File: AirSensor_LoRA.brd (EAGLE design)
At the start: 37.8 x 29.7 mm, 6 parts, among them U2 RFM95W-915S2

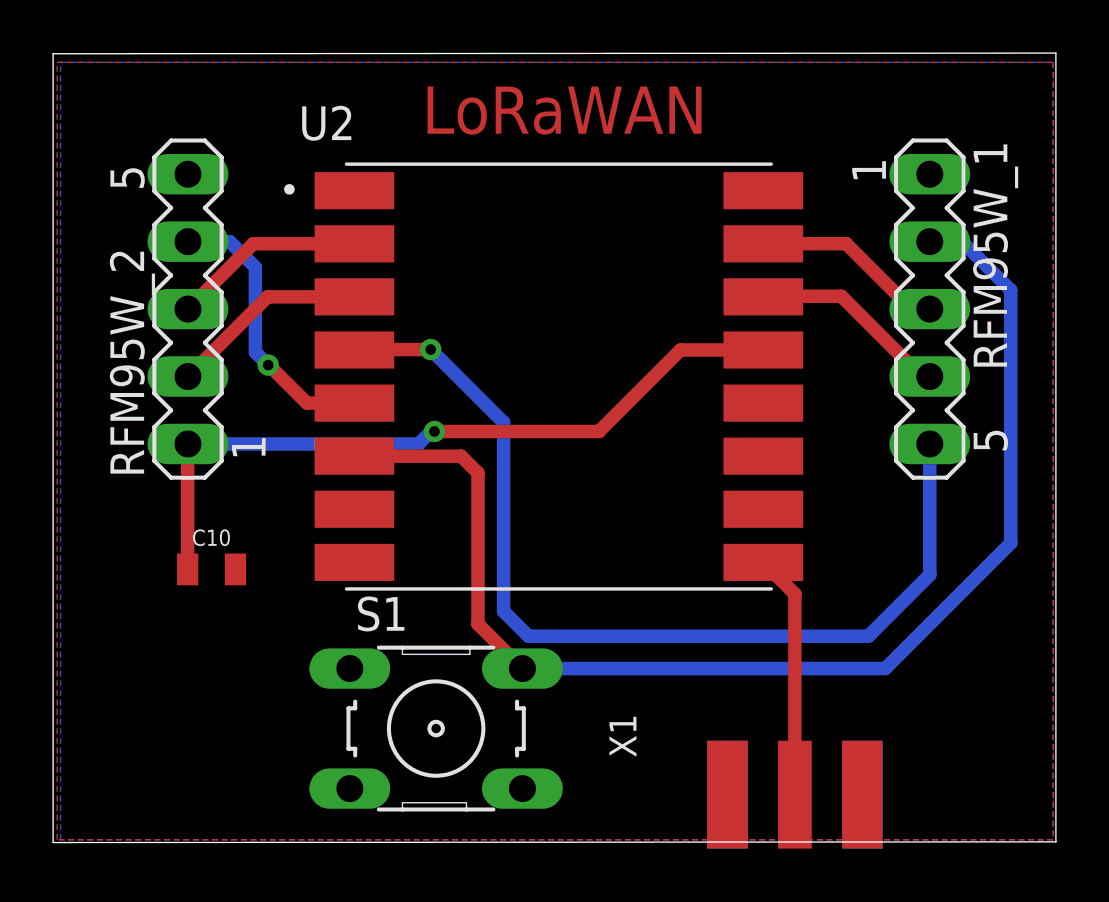
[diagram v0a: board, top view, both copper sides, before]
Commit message: added JTAG schematic and PCB  + all pictures
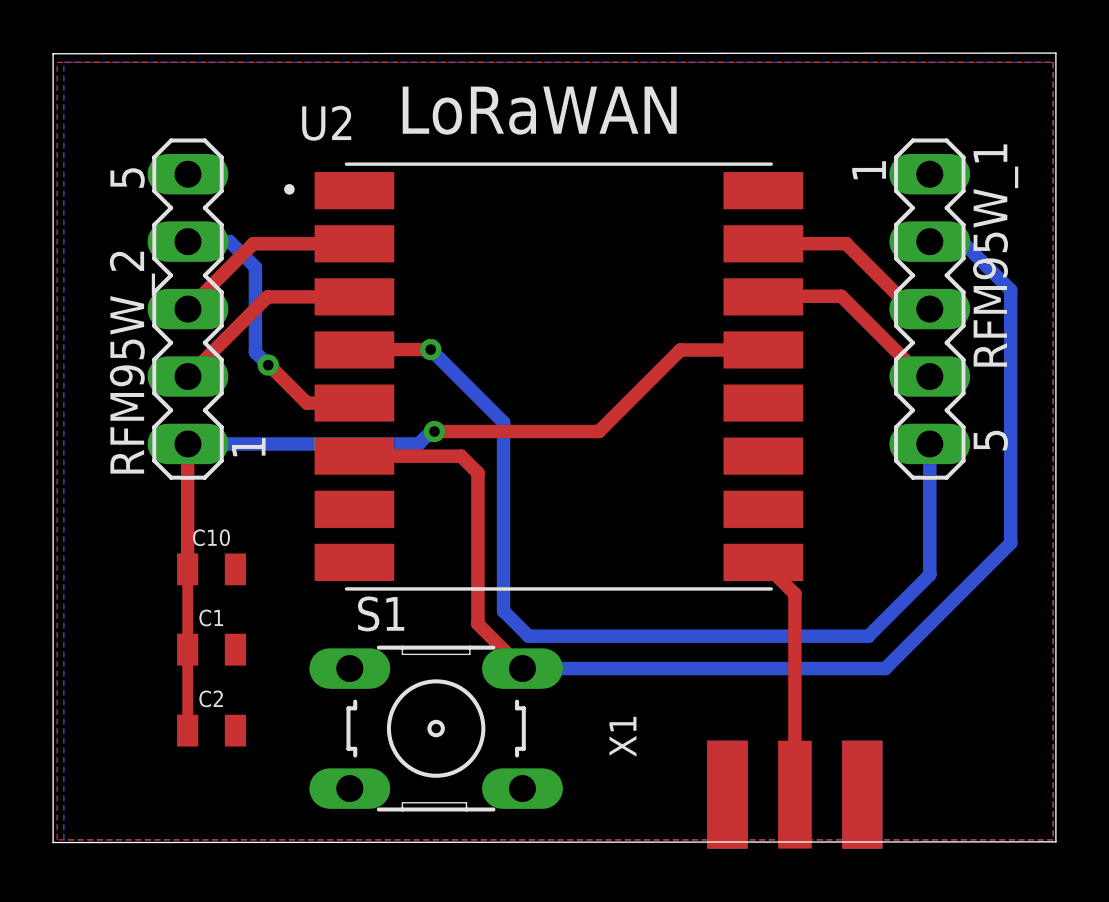
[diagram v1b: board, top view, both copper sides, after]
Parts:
- added C1: 1uF, SparkFun-Capacitors:0805
- added C2: 10uF, SparkFun-Capacitors:0805
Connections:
- net GND: now also C1.2, C2.2
- net N$17: now also C1.1, C2.1
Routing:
- net N$17: track 27.9 -> 34.0 mm
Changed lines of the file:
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@@
 <setting verticaltext="up"/>
 </settings>
-<grid distance="10" unitdist="mil" unit="mil" style="dots" multiple="1" display="yes" altdistance="5" altunitdist="mil" altunit="mm"/>
+<grid distance="5" unitdist="mil" unit="mil" style="dots" multiple="1" display="yes" altdistance="5" altunitdist="mil" altunit="mm"/>
 <layers>
 <layer number="1" name="Top" color="4" fill="1" visible="yes" active="yes"/>
@@
 <layer number="43" name="vRestrict" color="2" fill="10" visible="yes" active="yes"/>
 <layer number="44" name="Drills" color="7" fill="1" visible="no" active="yes"/>
-<layer number="45" name="Holes" color="7" fill="1" visible="no" active="yes"/>
+<layer number="45" name="Holes" color="7" fill="1" visible="yes" active="yes"/>
 <layer number="46" name="Milling" color="3" fill="1" visible="no" active="yes"/>
 <layer number="47" name="Measures" color="7" fill="1" visible="no" active="yes"/>
@@
 </layers>
 <board>
+<fusionsync huburn="a.YnVzaW5lc3M6c2t5bmV0MTMz" projecturn="a.YnVzaW5lc3M6c2t5bmV0MTMzI0QyMDE5MTAzMTIzMzQxNDY3Ng" f3durn="urn:adsk.wipprod:dm.lineage:gBG1N-XqQO-DzMLJpc-8hg" pcbguid="713ceda1-754c-4077-b978-a9e63d735a61" lastpulledtime="" lastsyncedchangeguid="" latestrevisionid="c9c4a9db-c59c-4e5b-af83-e9ca314a6cc9" lastsyncedrevisionid="c9c4a9db-c59c-4e5b-af83-e9ca314a6cc9" lastboardhashguid="1a8cda24-f025-4226-e9cc-3dac7828f5c5" lastpushedtime="2020-10-21T16:33:23Z" linktopcb3d="true"/>
 <plain>
 <wire x1="0" y1="52.2986" x2="37.77" y2="52.324" width="0" layer="20"/>
@@
 <wire x1="37.77" y1="82.032" x2="0" y2="82.0066" width="0" layer="20"/>
 <wire x1="0" y1="82.0066" x2="0" y2="52.2986" width="0" layer="20"/>
-<dimension x1="5.08" y1="77.47" x2="33.02" y2="77.47" x3="19.05" y3="82.8548" textsize="1.778" layer="1"/>
-<dimension x1="5.08" y1="77.4446" x2="5.08" y2="52.2732" x3="-2.3876" y3="64.8589" textsize="1.778" layer="1"/>
-<text x="24.638" y="80.772" size="1.778" layer="1" rot="R180">LoRaWAN</text>
+<text x="12.954" y="78.994" size="1.778" layer="25">LoRaWAN</text>
 </plain>
 <attributes>
@@
 <attribute name="VALUE" x="35.56" y="57.15" size="0.8128" layer="27" ratio="10" rot="R270"/>
 </element>
+<element name="C1" library="SparkFun-Capacitors" library_urn="urn:adsk.eagle:library:510" package="0805" package3d_urn="urn:adsk.eagle:package:37429/1" value="1uF" x="5.969" y="59.563" smashed="yes">
+<attribute name="NAME" x="5.969" y="60.452" size="0.6096" layer="25" font="vector" ratio="20" align="bottom-center"/>
+<attribute name="PROD_ID" value="CAP-08064" x="6.223" y="59.563" size="1.778" layer="27" display="off"/>
+<attribute name="VALUE" x="5.969" y="58.674" size="0.6096" layer="27" font="vector" ratio="20" align="top-center"/>
+</element>
+<element name="C2" library="SparkFun-Capacitors" library_urn="urn:adsk.eagle:library:510" package="0805" package3d_urn="urn:adsk.eagle:package:37429/1" value="10uF" x="5.969" y="56.515" smashed="yes">
+<attribute name="NAME" x="5.969" y="57.404" size="0.6096" layer="25" font="vector" ratio="20" align="bottom-center"/>
+<attribute name="PROD_ID" value="CAP-08064" x="6.223" y="56.515" size="1.778" layer="27" display="off"/>
+<attribute name="VALUE" x="5.969" y="55.626" size="0.6096" layer="27" font="vector" ratio="20" align="top-center"/>
+</element>
 </elements>
 <signals>
@@
 </polygon>
 <polygon width="0.254" layer="16" isolate="0.3048">
-<vertex x="0.2794" y="81.6864"/>
+<vertex x="0.4064" y="81.6864"/>
 <vertex x="37.6682" y="81.6864"/>
 <vertex x="37.6682" y="52.4002"/>
-<vertex x="0.2794" y="52.4002"/>
+<vertex x="0.4064" y="52.4002"/>
 </polygon>
+<contactref element="C1" pad="2"/>
+<contactref element="C2" pad="2"/>
 </signal>
 <signal name="3.3V">
@@
 <wire x1="23.6314" y1="70.85" x2="26.75" y2="70.85" width="0.508" layer="1"/>
 <wire x1="20.5613" y1="67.7799" x2="23.6314" y2="70.85" width="0.508" layer="1"/>
+<contactref element="C1" pad="1"/>
+<contactref element="C2" pad="1"/>
+<wire x1="5.069" y1="62.5856" x2="5.069" y2="59.563" width="0.4064" layer="1"/>
+<wire x1="5.069" y1="59.563" x2="5.069" y2="56.515" width="0.4064" layer="1"/>
 </signal>
 <signal name="N$18">
@@
 </note>
 <note version="8.3" severity="warning">
+Since Version 8.3, EAGLE supports Fusion synchronisation.
+This feature will not be available in this version and saving
+the document will break the link to the Fusion PCB feature.
+</note>
+<note version="8.3" severity="warning">
